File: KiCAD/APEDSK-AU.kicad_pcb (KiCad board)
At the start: 4 copper layers, 71.1 x 68.6 mm, 26 parts, among them J1 240-44-44Pins, P1 Power, P2 Analog, P3 Digital, P4 Digital, U1 74LS245, U2 74LS541, U3 74LS541, U4 GAL16V8, U5 74HC595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

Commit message: Silkscreen update
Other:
- board text added: "74HC595"
- board text added: "74HCT595"
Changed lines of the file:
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@@
   (general
     (thickness 1.6)
-    (drawings 86)
+    (drawings 88)
     (tracks 915)
     (zones 0)
@@
       (rotate (xyz 0 0 180))
     )
+  )
+  (gr_text 74HC595 (at 146.558 111.125 270) (layer F.SilkS)
+    (effects (font (size 1 1) (thickness 0.15)))
+  )
+  (gr_text 74HCT595 (at 146.558 84.455 270) (layer F.SilkS)
+    (effects (font (size 1 1) (thickness 0.15)))
   )
   (gr_text A0 (at 109.728 92.075) (layer B.SilkS)
@@
   (segment (start 113.443001 116.110001) (end 111.703999 116.110001) (width 0.25) (layer Top-Data) (net 26))
   (segment (start 147.141599 71.449988) (end 163.752937 71.449988) (width 0.25) (layer Top-Data) (net 26))
+  (segment (start 168.148 76.835) (end 168.148 84.455) (width 0.25) (layer Top-Data) (net 26))
   (segment (start 112.268 117.475) (end 113.632999 116.110001) (width 0.25) (layer Layer3-Address) (net 27) (status 10))
   (segment (start 114.808 113.665) (end 122.880652 113.665) (width 0.25) (layer Layer3-Address) (net 27))
@@
   (segment (start 166.385999 75.703766) (end 166.385999 112.887001) (width 0.25) (layer Top-Data) (net 61))
   (segment (start 147.828 120.015) (end 147.828 112.395) (width 0.25) (layer Top-Data) (net 61))
+  (segment (start 165.608 86.995) (end 168.148 89.535) (width 0.25) (layer Layer3-Address) (net 61))
+  (segment (start 165.608 75.565) (end 165.608 86.995) (width 0.25) (layer Layer3-Address) (net 61))
+  (segment (start 155.303001 74.439999) (end 164.482999 74.439999) (width 0.25) (layer Layer3-Address) (net 61))
+  (segment (start 164.482999 74.439999) (end 165.608 75.565) (width 0.25) (layer Layer3-Address) (net 61))
   (segment (start 137.668 114.935) (end 142.748 109.855) (width 0.25) (layer Layer3-Address) (net 62) (status 20))
   (segment (start 136.398 114.935) (end 137.668 114.935) (width 0.25) (layer Layer3-Address) (net 62) (status 10))
@@
   (segment (start 170.61699 104.84601) (end 168.847999 106.615001) (width 0.25) (layer Top-Data) (net 81) (status 20))
   (segment (start 169.418 126.365) (end 169.418 121.285) (width 0.25) (layer Top-Data) (net 81) (status 30))
+  (segment (start 156.718 88.265) (end 155.448 89.535) (width 0.25) (layer Layer2-Power) (net 81))
+  (segment (start 166.878 88.265) (end 156.718 88.265) (width 0.25) (layer Layer2-Power) (net 81))
+  (segment (start 169.418 85.725) (end 166.878 88.265) (width 0.25) (layer Layer2-Power) (net 81))
+  (segment (start 171.958 85.725) (end 169.418 85.725) (width 0.25) (layer Layer2-Power) (net 81))
   (segment (start 168.271501 117.475) (end 163.068 117.475) (width 0.25) (layer Layer3-Address) (net 82) (status 20))
   (segment (start 123.8504 78.105) (end 126.238 75.7174) (width 0.25) (layer Layer3-Address) (net 82) (status 10))
@@
   (segment (start 165.731501 71.755) (end 169.418 75.441499) (width 0.25) (layer Layer3-Address) (net 82))
   (segment (start 166.878 126.365) (end 163.068 122.555) (width 0.25) (layer Layer2-Power) (net 83) (status 30))
-  (segment (start 168.148 76.835) (end 168.148 84.455) (width 0.25) (layer Top-Data) (net 26))
-  (segment (start 165.608 86.995) (end 168.148 89.535) (width 0.25) (layer Layer3-Address) (net 61))
-  (segment (start 165.608 75.565) (end 165.608 86.995) (width 0.25) (layer Layer3-Address) (net 61))
-  (segment (start 155.303001 74.439999) (end 164.482999 74.439999) (width 0.25) (layer Layer3-Address) (net 61))
-  (segment (start 164.482999 74.439999) (end 165.608 75.565) (width 0.25) (layer Layer3-Address) (net 61))
-  (segment (start 156.718 88.265) (end 155.448 89.535) (width 0.25) (layer Layer2-Power) (net 81))
-  (segment (start 166.878 88.265) (end 156.718 88.265) (width 0.25) (layer Layer2-Power) (net 81))
-  (segment (start 169.418 85.725) (end 166.878 88.265) (width 0.25) (layer Layer2-Power) (net 81))
-  (segment (start 171.958 85.725) (end 169.418 85.725) (width 0.25) (layer Layer2-Power) (net 81))
   (segment (start 117.348 94.615) (end 114.808 92.075) (width 0.25) (layer Layer2-Power) (net 84) (status 20))
   (segment (start 117.348 127.635) (end 117.348 94.615) (width 0.25) (layer Layer2-Power) (net 84))

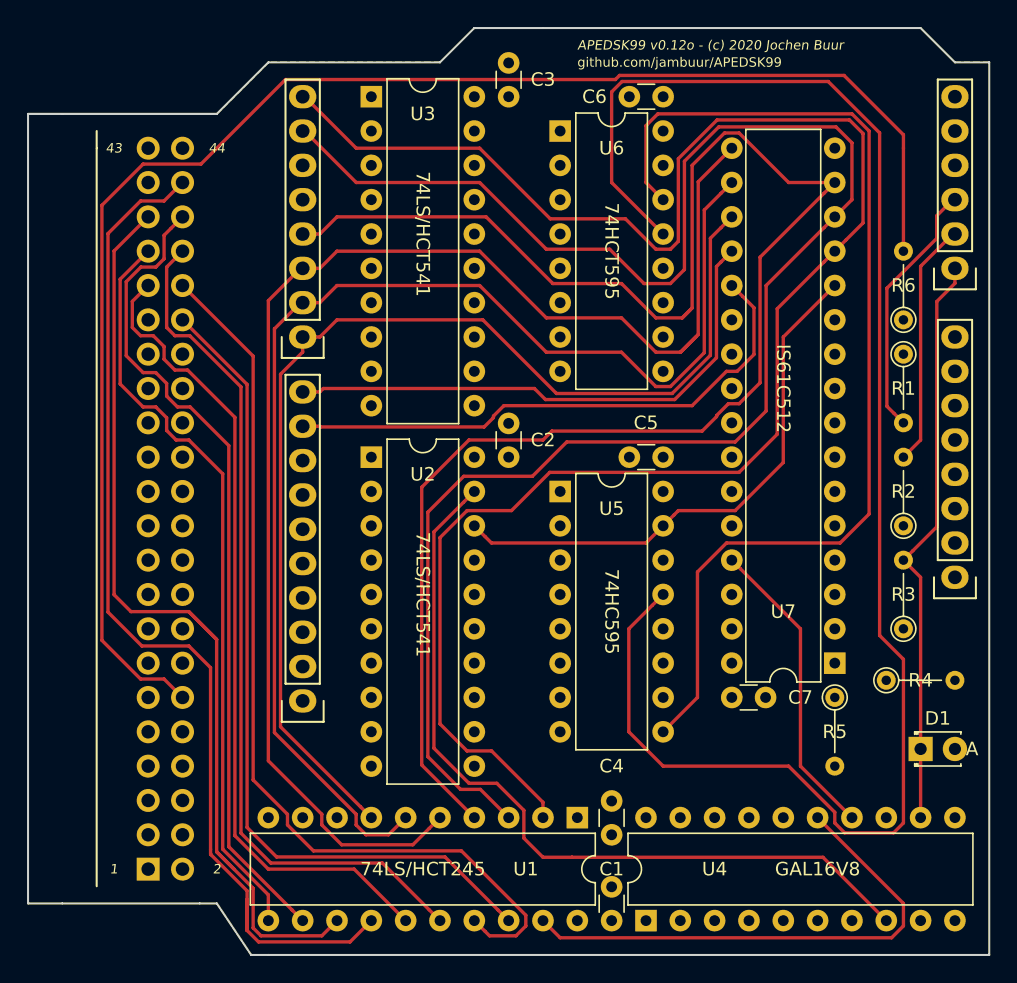
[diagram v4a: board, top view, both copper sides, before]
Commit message: KiCad V6 / D2
Migrated project to KiCad v6
Replaced R6 with D2 to remove video interference
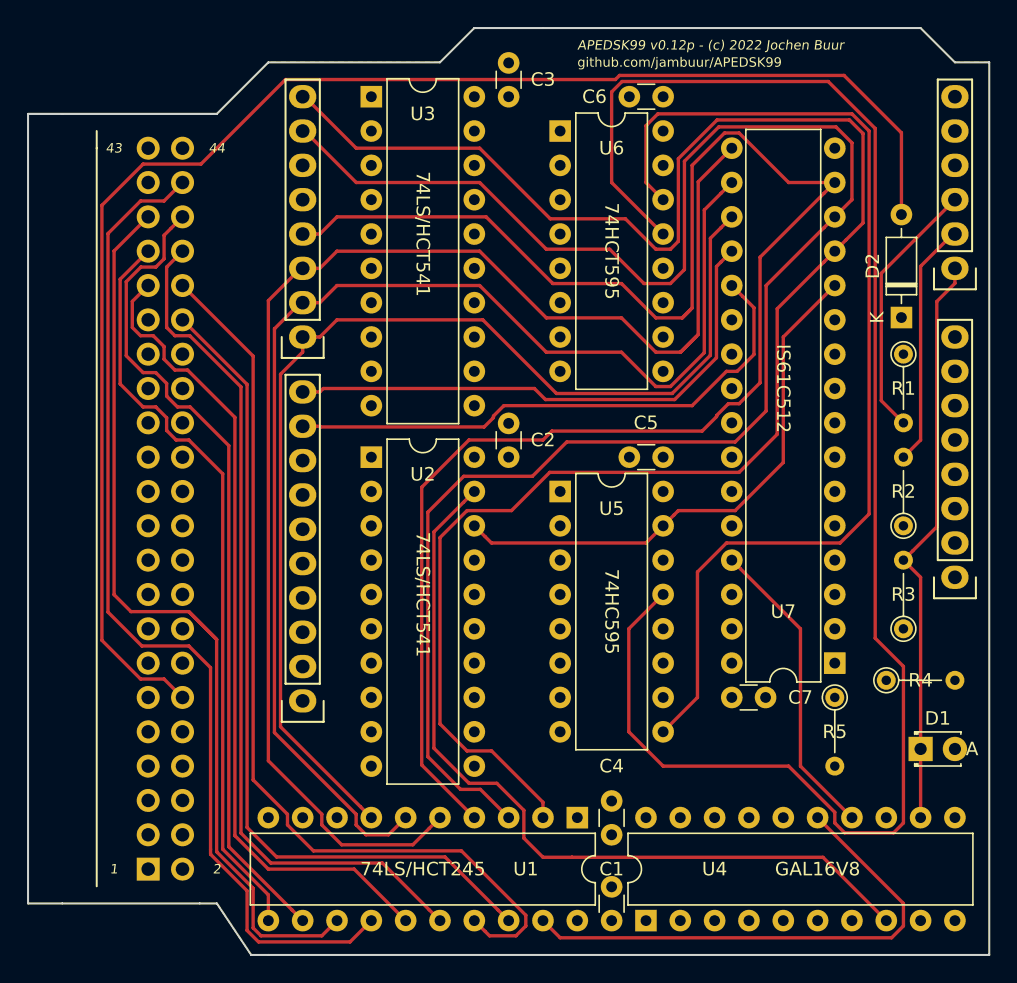
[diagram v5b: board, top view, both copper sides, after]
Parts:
- removed R6: 1K, Resistor_THT:R_Axial_DIN0204_L3.6mm_D1.6mm_P5.08mm_Vertical
- added D2: 1N4148, Diode_THT:D_DO-35_SOD27_P7.62mm_Horizontal, F.Cu at (168.0, 89.4)
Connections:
- net /~AD_CE renamed /~{AD_CE}
- net /~AD_WE renamed /~{AD_WE}
- net /~AR_BUF renamed /~{AR_BUF}
- net /~MEMEN renamed /~{MEMEN}
- net /~TIBUF renamed /~{TIBUF}
- net /~TI_INT renamed /~{TI_INT}
- net /~WE renamed /~{WE}
- J1 pad 1: Net-(J1-Pad1) -> unconnected-(J1-Pad1)
- J1 pad 13: Net-(J1-Pad13) -> unconnected-(J1-Pad13)
- J1 pad 2: Net-(J1-Pad2) -> unconnected-(J1-Pad2)
- J1 pad 22: Net-(J1-Pad22) -> unconnected-(J1-Pad22)
- J1 pad 24: Net-(J1-Pad24) -> unconnected-(J1-Pad24)
- J1 pad 28: Net-(J1-Pad28) -> unconnected-(J1-Pad28)
- J1 pad 3: Net-(J1-Pad3) -> unconnected-(J1-Pad3)
- J1 pad 33: Net-(J1-Pad33) -> unconnected-(J1-Pad33)
- J1 pad 4: Net-(J1-Pad4) -> unconnected-(J1-Pad4)
- J1 pad 41: Net-(J1-Pad41) -> unconnected-(J1-Pad41)
- J1 pad 43: Net-(J1-Pad43) -> unconnected-(J1-Pad43)
- J1 pad 44: Net-(J1-Pad44) -> unconnected-(J1-Pad44)
- P1 pad 1: Net-(P1-Pad1) -> unconnected-(P1-Pad1)
- P1 pad 2: Net-(P1-Pad2) -> unconnected-(P1-Pad2)
- P1 pad 3: Net-(P1-Pad3) -> unconnected-(P1-Pad3)
- P1 pad 4: Net-(P1-Pad4) -> unconnected-(P1-Pad4)
- P1 pad 8: Net-(P1-Pad8) -> unconnected-(P1-Pad8)
- P3 pad 1: Net-(P3-Pad1) -> unconnected-(P3-Pad1)
- P3 pad 10: /AD_D6 -> /AD_D0
- P3 pad 2: Net-(P3-Pad2) -> unconnected-(P3-Pad2)
- P3 pad 3: Net-(P3-Pad3) -> unconnected-(P3-Pad3)
- P3 pad 4: Net-(P3-Pad4) -> unconnected-(P3-Pad4)
- P3 pad 5: Net-(P3-Pad5) -> unconnected-(P3-Pad5)
- P3 pad 6: Net-(P3-Pad6) -> unconnected-(P3-Pad6)
- P3 pad 7: Net-(P3-Pad7) -> unconnected-(P3-Pad7)
- P3 pad 8: Net-(P3-Pad8) -> unconnected-(P3-Pad8)
- P3 pad 9: /AD_D7 -> /AD_D0
- P4 pad 1: /AD_D5 -> /AD_D0
- P4 pad 2: /AD_D4 -> /AD_D0
- P4 pad 3: /AD_D3 -> /AD_D0
- P4 pad 4: /AD_D2 -> /AD_D0
- P4 pad 7: /AD_D1 -> /AD_D0
- U1 pad 3: /AD_D1 -> /AD_D0
- U1 pad 4: /AD_D2 -> /AD_D0
- U1 pad 5: /AD_D3 -> /AD_D0
- U1 pad 6: /AD_D4 -> /AD_D0
- U1 pad 7: /AD_D5 -> /AD_D0
- U1 pad 8: /AD_D6 -> /AD_D0
- U1 pad 9: /AD_D7 -> /AD_D0
- U2 pad 11: /AD_A7 -> /AD_A0
- U2 pad 12: /AD_A6 -> /AD_A0
- U2 pad 13: /AD_A5 -> /AD_A0
- U2 pad 14: /AD_A4 -> /AD_A0
- U2 pad 15: /AD_A3 -> /AD_A0
- U2 pad 16: /AD_A2 -> /AD_A0
- U2 pad 17: /AD_A1 -> /AD_A0
- U3 pad 11: /AD_A15 -> /AD_A10
- U3 pad 12: /AD_A14 -> /AD_A10
- U3 pad 13: /AD_A13 -> /AD_A10
- U3 pad 14: /AD_A12 -> /AD_A10
- U3 pad 15: /AD_A11 -> /AD_A10
- U3 pad 17: /AD_A9 -> /AD_A10
- U3 pad 18: /AD_A8 -> /AD_A10
- U4 pad 16: Net-(U4-Pad16) -> unconnected-(U4-Pad16)
- U4 pad 17: Net-(U4-Pad17) -> unconnected-(U4-Pad17)
- U4 pad 18: Net-(U4-Pad18) -> unconnected-(U4-Pad18)
- U4 pad 19: Net-(U4-Pad19) -> unconnected-(U4-Pad19)
- U4 pad 2: /AD_A13 -> /AD_A10
- U4 pad 3: /AD_A14 -> /AD_A10
- U4 pad 4: /AD_A15 -> /AD_A10
- U5 pad 1: /AD_A1 -> /AD_A0
- U5 pad 2: /AD_A2 -> /AD_A0
- U5 pad 3: /AD_A3 -> /AD_A0
- U5 pad 4: /AD_A4 -> /AD_A0
- U5 pad 5: /AD_A5 -> /AD_A0
- U5 pad 6: /AD_A6 -> /AD_A0
- U5 pad 7: /AD_A7 -> /AD_A0
- U6 pad 1: /AD_A9 -> /AD_A10
- U6 pad 15: /AD_A8 -> /AD_A10
- U6 pad 3: /AD_A11 -> /AD_A10
- U6 pad 4: /AD_A12 -> /AD_A10
- U6 pad 5: /AD_A13 -> /AD_A10
- U6 pad 6: /AD_A14 -> /AD_A10
- U6 pad 7: /AD_A15 -> /AD_A10
- U6 pad 9: Net-(U6-Pad9) -> unconnected-(U6-Pad9)
- U7 pad 1: Net-(U7-Pad1) -> unconnected-(U7-Pad1)
- U7 pad 10: /AD_A2 -> /AD_A0
- U7 pad 11: /AD_A1 -> /AD_A0
- U7 pad 14: /AD_D1 -> /AD_D0
- U7 pad 15: /AD_D2 -> /AD_D0
- U7 pad 17: /AD_D3 -> /AD_D0
- U7 pad 18: /AD_D4 -> /AD_D0
- U7 pad 19: /AD_D5 -> /AD_D0
- U7 pad 2: Net-(U7-Pad2) -> unconnected-(U7-Pad2)
- U7 pad 20: /AD_D6 -> /AD_D0
- U7 pad 21: /AD_D7 -> /AD_D0
- U7 pad 25: /AD_A11 -> /AD_A10
- U7 pad 26: /AD_A9 -> /AD_A10
- U7 pad 27: /AD_A8 -> /AD_A10
- U7 pad 28: /AD_A13 -> /AD_A10
- U7 pad 3: /AD_A14 -> /AD_A10
- U7 pad 31: /AD_A15 -> /AD_A10
- U7 pad 4: /AD_A12 -> /AD_A10
- U7 pad 5: /AD_A7 -> /AD_A0
- U7 pad 6: /AD_A6 -> /AD_A0
- U7 pad 7: /AD_A5 -> /AD_A0
- U7 pad 8: /AD_A4 -> /AD_A0
- U7 pad 9: /AD_A3 -> /AD_A0
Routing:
- net /AD_D0: track 132.0 -> 821.0 mm
- net /AD_A10: track 36.4 -> 567.1 mm
- net /AD_A0: track 93.5 -> 458.8 mm
- net /AD_D1: track 131.8 -> 0.00 mm
- net /AD_D2: track 128.7 -> 0.00 mm
- net /AD_D3: track 104.1 -> 0.00 mm
- net /AD_A14: track 102.1 -> 0.00 mm
- net /AD_A12: track 97.3 -> 0.00 mm
- net /AD_A15: track 95.9 -> 0.00 mm
- net /AD_D4: track 94.4 -> 0.00 mm
- net /AD_A13: track 91.8 -> 0.00 mm
- net /AD_D5: track 84.0 -> 0.00 mm
- net /AD_D6: track 73.3 -> 0.00 mm
- net /AD_D7: track 72.6 -> 0.00 mm
- net /AD_A8: track 60.8 -> 0.00 mm
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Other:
- net class Default removed
- board text added: "APEDSK99 v0.12p - (c) 2022 Jochen Buur"
- board text added: "~{AB}"
- board text added: "~{CE}"
- board text added: "~{INT}"
- board text added: "~{MEMEN}"
- board text added: "~{TB}"
- board text added: "~{WE}"
- board text removed: "APEDSK99 v0.12o - (c) 2020 Jochen Buur"
- board text removed: "~AB"
- board text removed: "~CE"
- board text removed: "~INT"
- board text removed: "~MEMEN"
- board text removed: "~TB"
- board text removed: "~WE"
